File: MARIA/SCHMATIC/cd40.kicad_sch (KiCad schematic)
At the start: 14 parts

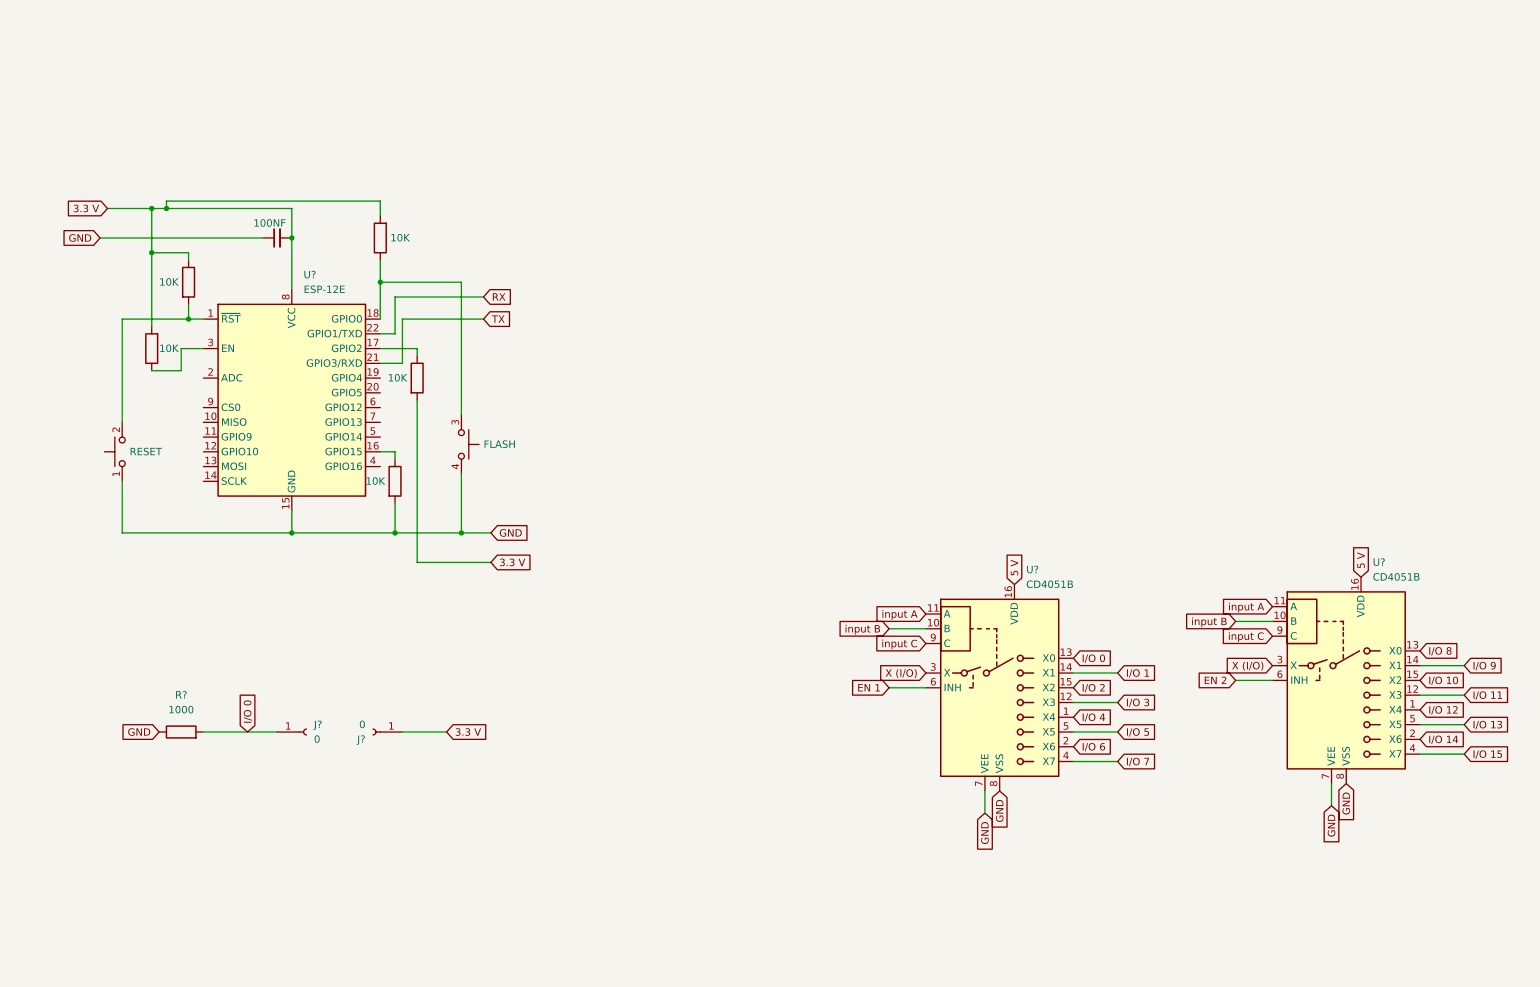
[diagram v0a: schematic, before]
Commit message: 16 PADS ADDED
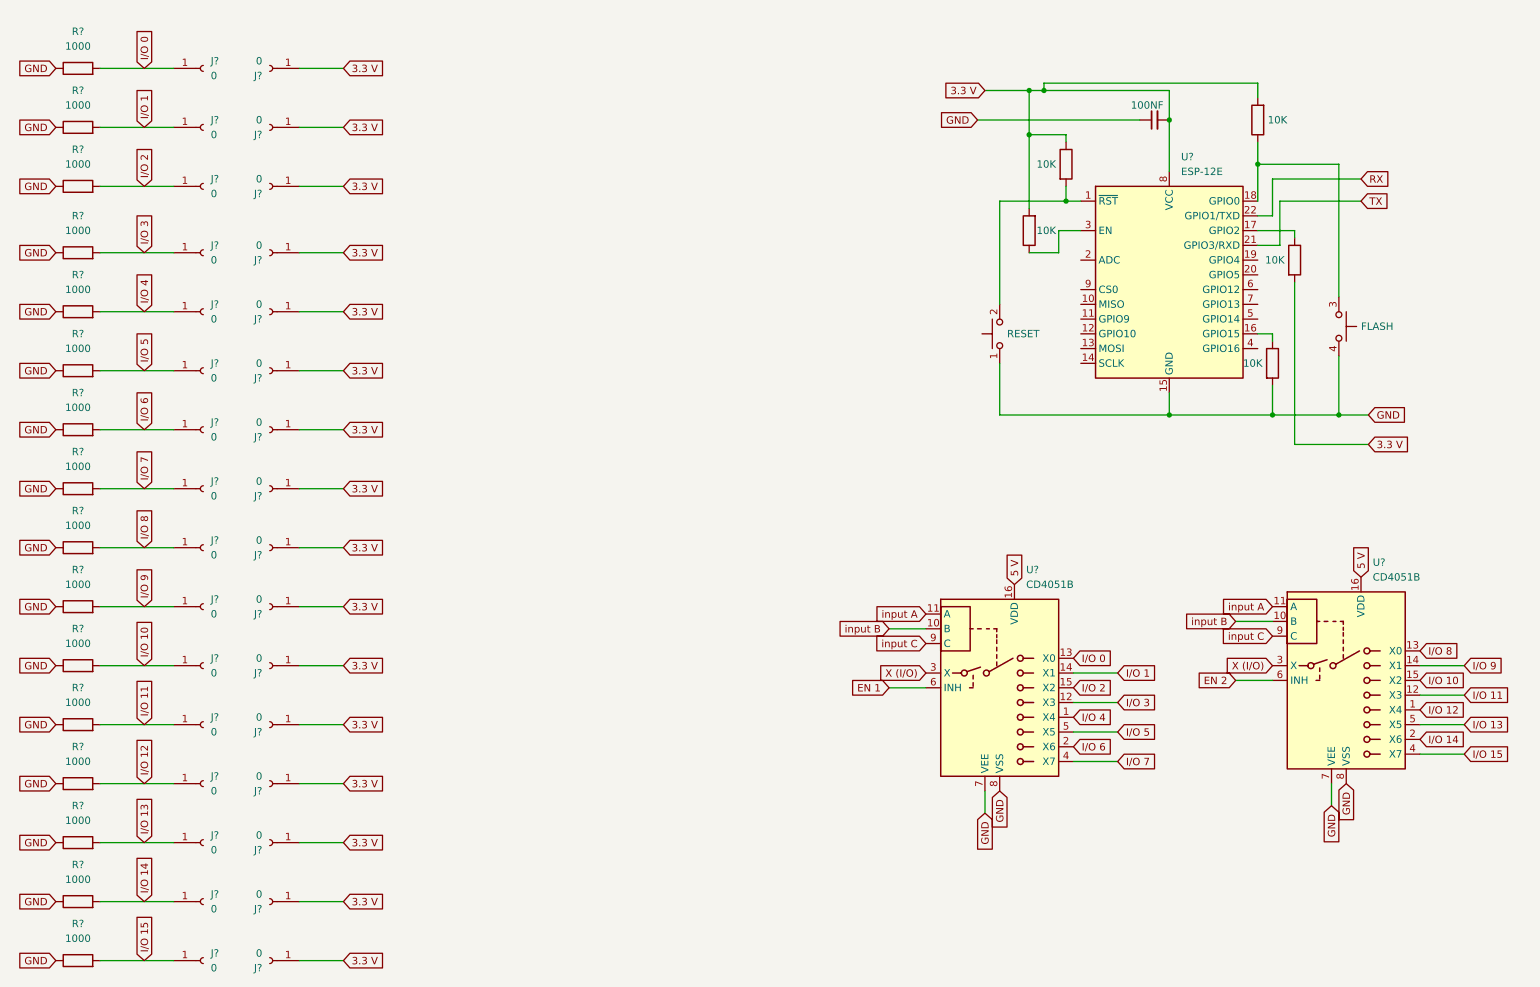
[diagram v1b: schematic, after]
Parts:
- added J? (x30): 0, symbol Connector:Conn_01x01_Female
- added R? (x15): 1000, symbol Device:R
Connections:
- net 3.3 V: now also J?.1 (Pin_1), J?.1 (Pin_1), J?.1 (Pin_1), J?.1 (Pin_1), J?.1 (Pin_1), J?.1 (Pin_1), J?.1 (Pin_1), J?.1 (Pin_1), J?.1 (Pin_1), J?.1 (Pin_1), J?.1 (Pin_1), J?.1 (Pin_1), J?.1 (Pin_1), J?.1 (Pin_1), J?.1 (Pin_1)
- net GND: now also R?.1, R?.1, R?.1, R?.1, R?.1, R?.1, R?.1, R?.1, R?.1, R?.1, R?.1, R?.1, R?.1, R?.1, R?.1
- net I/O 1: now also J?.1 (Pin_1), R?.2
- net I/O 10: now also J?.1 (Pin_1), R?.2
- net I/O 11: now also J?.1 (Pin_1), R?.2
- net I/O 12: now also J?.1 (Pin_1), R?.2
- net I/O 13: now also J?.1 (Pin_1), R?.2
- net I/O 14: now also J?.1 (Pin_1), R?.2
- net I/O 15: now also J?.1 (Pin_1), R?.2
- net I/O 2: now also J?.1 (Pin_1), R?.2
- net I/O 3: now also J?.1 (Pin_1), R?.2
- net I/O 4: now also J?.1 (Pin_1), R?.2
- net I/O 5: now also J?.1 (Pin_1), R?.2
- net I/O 6: now also J?.1 (Pin_1), R?.2
- net I/O 7: now also J?.1 (Pin_1), R?.2
- net I/O 8: now also J?.1 (Pin_1), R?.2
- net I/O 9: now also J?.1 (Pin_1), R?.2
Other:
- moved on the sheet: J?, R?, U?
